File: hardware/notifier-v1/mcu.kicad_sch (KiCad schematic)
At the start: 22 parts, among them SW1 RESET, SW2 BOOT, SW3 BUTTON, U1 ESP32-S3-WROOM-1-N8R2

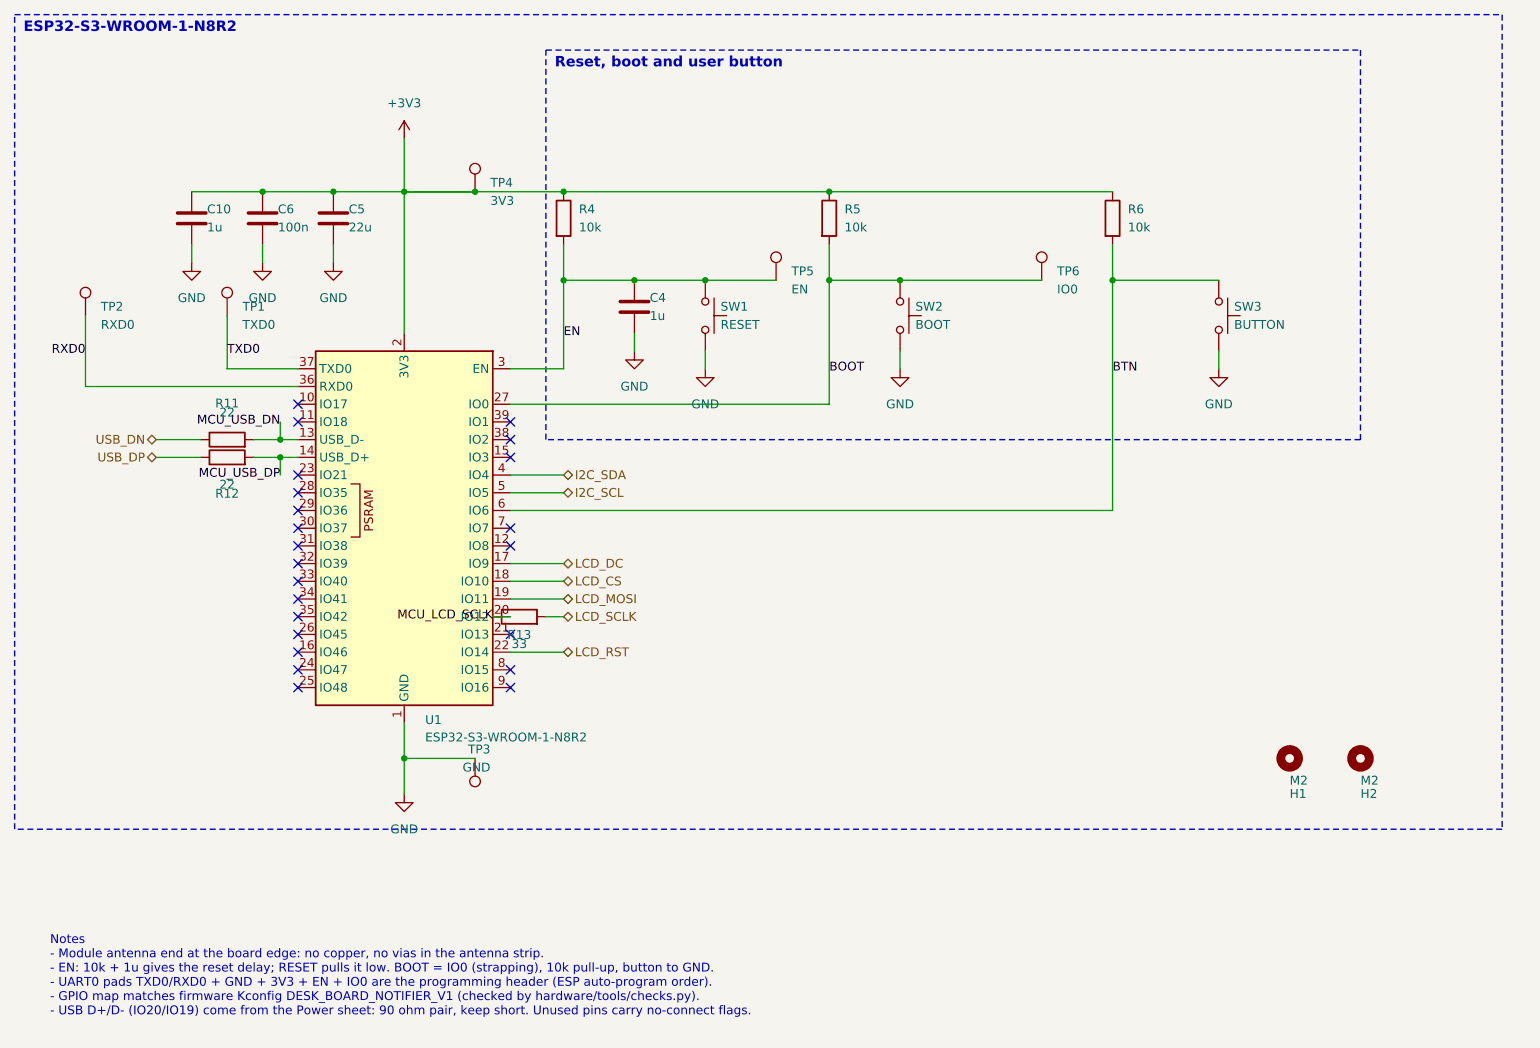
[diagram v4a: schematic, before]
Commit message: Layout A: USB-C on the back edge, corner mounts, no buttons, JLC fab data
- J2 display socket mirrored (1 RST 2 CS 3 DC 4 SDA 5 SCL 6 GND 7 VCC),
  face at the right edge
- USB-C J1 on the left edge (enclosure back), ESD/CC/fuse beside it,
  hand-drawn 0.27/0.15 pair (~91 ohm diff, tools/impedance.py), only
  GND under the shell (DRC rule area)
- SW1-SW3/R6/BTN removed; 1.5 mm debug pads TX RX 3V3 EN GND IO0;
  firmware DESK_BTN = -1 on notifier-v1
- Four M2 corner holes with keepouts; sensor island grown to 14.8 mm
  with H3 in its corner, re-hand-routed (BME688/SHT40 8.9 mm apart)
- I2C >= 1.6 mm from USB on the same layer; vias >= 0.15 mm from
  same-net SMD pads (rule), hand vias >= 0.2 mm
- Silk "v1 ${GIT_SHA}" resolved at fab export; JLC order-number mark
- Fab: Protel gerbers without X2, PTH/NPTH split, JLC BOM/CPL, CPL
  rotation fixes (U4 +90, U5 +270); pipeline --fab-only on a clean
  commit; route retry until the gate passes
- ORDER.md: stackup JLC04161H-7628, rails left/right, preview checklist,
  bring-up without buttons; PLAN.md enclosure notes

Co-Authored-By: Claude Opus 5.5 <noreply@anthropic.com>
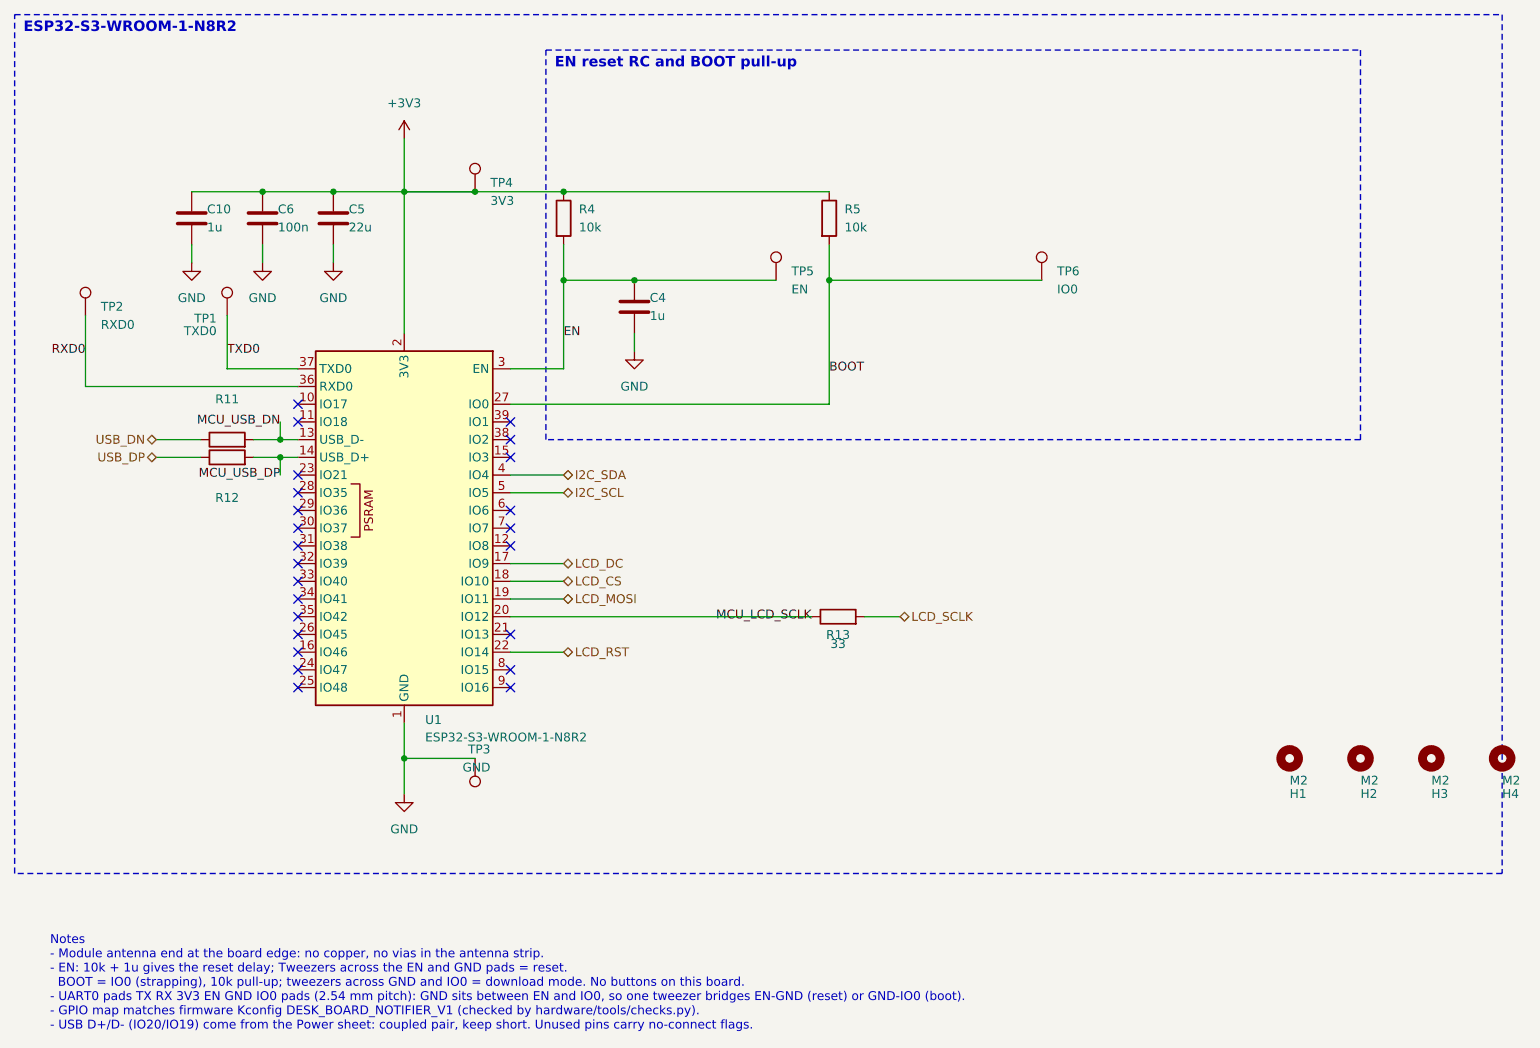
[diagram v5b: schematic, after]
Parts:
- removed R6: 10k, Resistor_SMD:R_0402_1005Metric, symbol Device:R
- removed SW1: RESET, Button_Switch_SMD:SW_Push_1P1T_XKB_TS-1187A, symbol Switch:SW_Push
- removed SW2: BOOT, Button_Switch_SMD:SW_Push_1P1T_XKB_TS-1187A, symbol Switch:SW_Push
- removed SW3: BUTTON, Button_Switch_SMD:SW_Push_1P1T_XKB_TS-1187A, symbol Switch:SW_Push
- added H3, H4: M2, MountingHole:MountingHole_2.2mm_M2, symbol Mechanical:MountingHole
- TP1, TP2, TP3, TP4, TP5, TP6: footprint TestPoint:TestPoint_Pad_D1.0mm -> TestPoint:TestPoint_Pad_D1.5mm
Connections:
- net BTN: no longer names the net of U1.6 (IO6)
- no-connect marks 23 -> 24
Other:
- note added: "EN reset RC and BOOT pull-up"
- note added: "Notes - Module antenna end at the board edge: no copper, no vias in the antenna strip. - EN: 10k + 1u gives the reset delay; Tweezers across the EN and GND pads = reset. BOOT = IO0 (strapping), 10k pull-up; tweezers across GND and IO0 = download mode. No buttons on this board. - UART0 pads TX RX 3V3 EN GND IO0 pads (2.54 mm pitch): GND sits between EN and IO0, so one tweezer bridges EN-GND (reset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"
- note removed: "Notes - Module antenna end at the board edge: no copper, no vias in the antenna strip. - EN: 10k + 1u gives the reset delay; RESET pulls it low. BOOT = IO0 (strapping), 10k pull-up, button to GND. - UART0 pads TXD0/RXD0 + GND + 3V3 + EN + IO0 are the programming header (ESP auto-program order). - GPIO map matches firmware Kconfig DESK_BOARD_NOTIFIER_V1 (checked by hardware/tools/checks.py). - USB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"
- note removed: "Reset, boot and user button"
